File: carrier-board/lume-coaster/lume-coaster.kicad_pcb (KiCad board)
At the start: 2 copper layers, 85 x 40 mm, 37 parts, among them J1_BOT T5AI_CORE_BOT, J1_TOP T5AI_CORE_TOP, J2 ILI9341_SPI_LCD, J3 ACTIVE_CHIME, J4_HARNESS TO_MODULE_CN1, J5 USB-C, Q1 AO3401, SW1 MODE, SW2 UP, SW3 DOWN

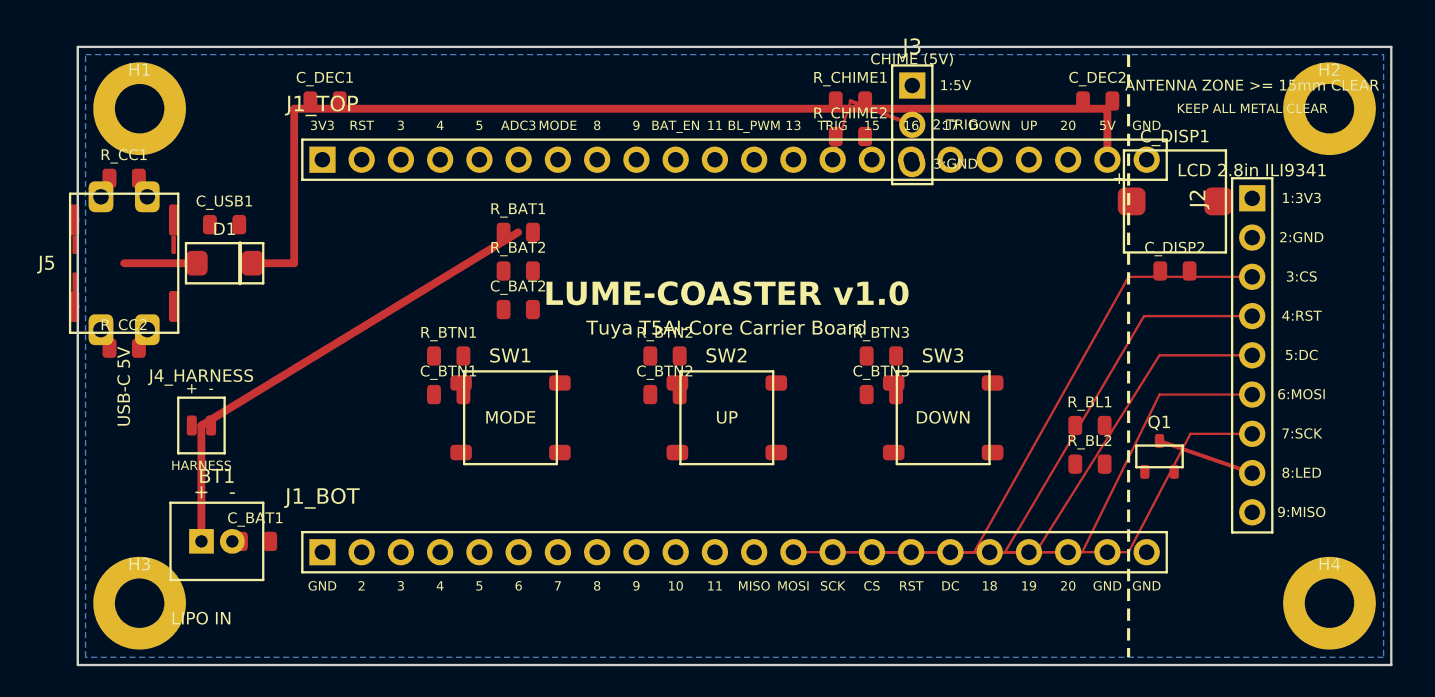
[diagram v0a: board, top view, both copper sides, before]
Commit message: feat(week1): lume-coaster carrier board - fab-ready
- Tuya T5AI-Core (T5-E1) carrier, 85x40mm 2-layer
- 2x1x22 PinSocket headers, 25.4mm center-to-center
- Full GND pour on B.Cu with on-disk filled polygon
- ERC 0/0/0, DRC 0 violations / 0 unconnected / 0 footprint errors
- Gerbers + drill archive verified (G36/G37 solid copper fill present)
- Untrack .history submodule, KiCad lockfiles, scratch generators
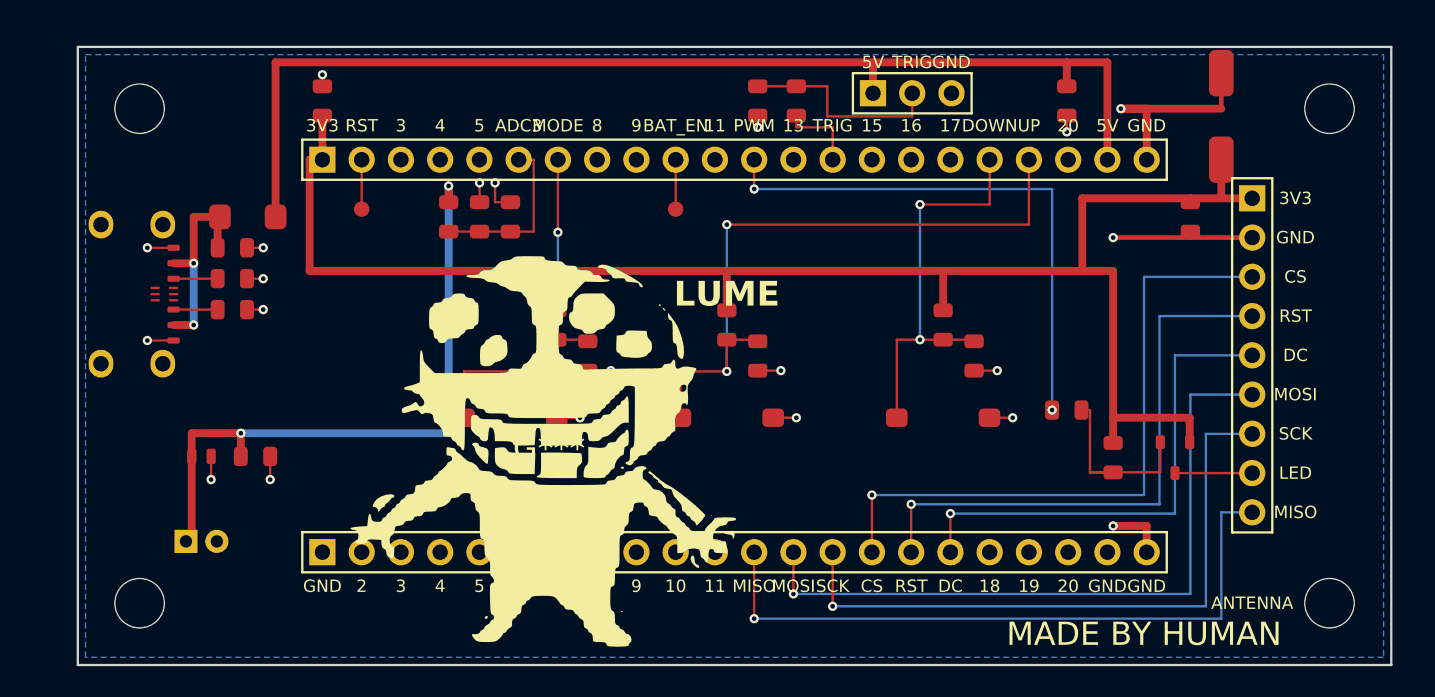
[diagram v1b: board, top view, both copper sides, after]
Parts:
- removed the J4_HARNESS at (8.00, 24.5)
- added G***: LOGO, LOGO, F.Cu at (30.5, 26.0)
- added J4_HARNESS: TO_MODULE_CN1, Connector_JST:JST_GH_SM02B-GHS-TB_1x02-1MP_P1.25mm_Horizontal, F.Cu at (8.00, 26.5)
- added TP1: BATT_EN, TestPoint:TestPoint_Pad_D1.0mm, F.Cu at (38.7, 10.5)
- added TP2: TS_RST, TestPoint:TestPoint_Pad_D1.0mm, F.Cu at (18.4, 10.5)
- C_BAT1, C_BAT2, C_BTN1, C_BTN2, C_BTN3, C_DEC1, C_DEC2, C_DISP2, C_USB1: footprint Resistor_SMD:R_0805_2012Metric -> Capacitor_SMD:C_0805_2012Metric
- H1, H2, H3, H4: value (none) -> MountingHole; footprint MountingHole:MountingHole_3.2mm_M3_Pad -> MountingHole:MountingHole_3.2mm_M3
- J3: footprint Connector_PinHeader_2.54mm:PinHeader_1x03_P2.54mm_Vertical -> Connector_PinHeader_2.54mm:PinHeader_1x03_P2.54mm_Horizontal
- Q1: value AO3401 -> AO3401A
- SW1, SW2, SW3: footprint Button_Switch_SMD:SW_Push_1P1T_NO_6x6mm_H9.5mm -> Button_Switch_SMD:SW_Push_1TS009xxxx-xxxx-xxxx_6x6x5mm
- moved J5 14.3 mm to (0.00, 0.00), turned to 0 degrees
- moved R_CC1 9.55 mm to (10.0, 15.0)
- moved C_BTN1 9.34 mm to (33.0, 20.0)
- moved R_CC2 7.43 mm to (10.0, 17.0)
- moved R_BTN1 7.28 mm to (31.0, 18.0)
- moved C_BTN2 6.50 mm to (44.0, 20.0)
- moved C_BTN3 6.50 mm to (58.0, 20.0)
- moved R_CHIME2 6.43 mm to (44.0, 3.50)
- moved C_DISP1 6.26 mm to (74.0, 4.50)
- moved C_BAT2 6.02 mm to (28.0, 11.0)
- moved C_BAT1 5.50 mm to (11.5, 26.5)
- moved R_BAT1 4.61 mm to (24.0, 11.0)
- moved R_BTN2 4.47 mm to (42.0, 18.0)
- moved R_BTN3 4.47 mm to (56.0, 18.0)
- moved R_BAT2 4.30 mm to (26.0, 11.0)
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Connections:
- net CC1 renamed /CC1
- net CC2 renamed /CC2
- net LCD_DC renamed /LCD_DC
- net LCD_LED renamed /LCD_LED
- net LCD_RST renamed /LCD_RST
- net SPI0_CS renamed /SPI0_CS
- net SPI0_MISO renamed /SPI0_MISO
- net SPI0_MOSI renamed /SPI0_MOSI
- net SPI0_SCK renamed /SPI0_SCK
- net VBAT renamed /VBAT
- BT1 pad 2: GND -> /GND
- C_BAT1 pad 2: GND -> /GND
- C_BAT2 pad 1: BATT_SENSE -> /GND
- C_BAT2 pad 2: GND -> /BATT_SENSE
- C_BTN1 pad 1: BTN_MODE -> /BTN_MODE
- C_BTN1 pad 2: GND -> /GND
- C_BTN2 pad 1: BTN_UP -> /BTN_UP
- C_BTN2 pad 2: GND -> /GND
- C_BTN3 pad 1: BTN_DOWN -> /BTN_DOWN
- C_BTN3 pad 2: GND -> /GND
- C_DEC1 pad 1: +3V3 -> /GND
- C_DEC1 pad 2: GND -> /+3V3
- C_DEC2 pad 1: +5V -> /+5V
- C_DEC2 pad 2: GND -> /GND
- C_DISP1 pad 1: +3V3 -> /+3V3
- C_DISP1 pad 2: GND -> /GND
- C_DISP2 pad 1: +3V3 -> /+3V3
- C_DISP2 pad 2: GND -> /GND
- C_USB1 pad 1: VBUS -> /VBUS
- C_USB1 pad 2: GND -> /GND
- D1 pad 1: VBUS -> /+5V
- D1 pad 2: +5V -> /VBUS
- J1_BOT pad 1: GND -> /GND
- J1_BOT pad 21: GND -> /GND
- J1_BOT pad 22: GND -> /GND
- J1_TOP pad 1: +3V3 -> /+3V3
- J1_TOP pad 10: BATT_EN -> /BATT_EN
- J1_TOP pad 12: LCD_BL_GATE -> /LCD_BL_PWM
- J1_TOP pad 14: CHIME_TRIG -> /CHIME_TRIG
- J1_TOP pad 18: BTN_DOWN -> /BTN_DOWN
- J1_TOP pad 19: BTN_UP -> /BTN_UP
- J1_TOP pad 2: TS_RST -> /TS_RST
- J1_TOP pad 21: +5V -> /+5V
- J1_TOP pad 22: GND -> /GND
- J1_TOP pad 6: BATT_SENSE -> /BATT_SENSE
- J1_TOP pad 7: BTN_MODE -> /BTN_MODE
- J2 pad 1: +3V3 -> /+3V3
- J2 pad 2: GND -> /GND
- J3 pad 1: +5V -> /+5V
- J3 pad 2: CHIME_OUT -> /CHIME_OUT
- J3 pad 3: GND -> /GND
- J5 pad A1: GND -> /GND
- J5 pad A12: GND -> /GND
- J5 pad A4: VBUS -> /VBUS
- J5 pad A8: GND -> (no net)
- J5 pad A9: VBUS -> /VBUS
- J5 pad B1: GND -> /GND
- J5 pad B12: GND -> /GND
- J5 pad B4: VBUS -> /VBUS
- J5 pad B9: VBUS -> /VBUS
- Q1 pad 1: LCD_BL_GATE -> /LCD_BL_GATE
- Q1 pad 2: +3V3 -> /+3V3
- R_BAT1 pad 2: BATT_SENSE -> /BATT_SENSE
- R_BAT2 pad 1: BATT_SENSE -> /GND
- R_BAT2 pad 2: GND -> /BATT_SENSE
- R_BL1 pad 1: LCD_BL_GATE -> /+3V3
- R_BL1 pad 2: +3V3 -> /LCD_BL_GATE
- R_BL2 pad 1: LCD_BL_GATE -> /LCD_BL_PWM
- R_BL2 pad 2: LCD_BL_GATE -> /LCD_BL_GATE
- R_BTN1 pad 1: BTN_MODE -> /+3V3
- R_BTN1 pad 2: +3V3 -> /BTN_MODE
- R_BTN2 pad 1: BTN_UP -> /+3V3
- R_BTN2 pad 2: +3V3 -> /BTN_UP
- R_BTN3 pad 1: BTN_DOWN -> /+3V3
- R_BTN3 pad 2: +3V3 -> /BTN_DOWN
- R_CC1 pad 2: GND -> /GND
- R_CC2 pad 2: GND -> /GND
- R_CHIME1 pad 1: CHIME_TRIG -> /CHIME_OUT
- R_CHIME1 pad 2: CHIME_OUT -> /CHIME_TRIG
- R_CHIME2 pad 1: CHIME_OUT -> /CHIME_OUT
- R_CHIME2 pad 2: GND -> /GND
- SW1 pad 1: BTN_MODE -> /BTN_MODE
- SW1 pad 2: BTN_MODE -> /GND
- SW2 pad 1: BTN_UP -> /BTN_UP
- SW2 pad 2: BTN_UP -> /GND
- SW3 pad 1: BTN_DOWN -> /BTN_DOWN
- SW3 pad 2: BTN_DOWN -> /GND
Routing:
- net /+3V3: track 0.00 -> 106.6 mm
- net /+5V: track 0.00 -> 73.7 mm
- net +5V: track 68.6 -> 0.00 mm
- net /GND: track 0.00 -> 51.6 mm, vias 0 -> 21
- net /SPI0_MISO: track 0.00 -> 43.4 mm, vias 0 -> 1
- net /BTN_UP: track 0.00 -> 43.4 mm, vias 0 -> 2
- net /LCD_BL_PWM: track 0.00 -> 35.5 mm, vias 0 -> 2
- net /BTN_MODE: track 0.00 -> 26.9 mm, vias 0 -> 2
- net /BTN_DOWN: track 0.00 -> 26.3 mm, vias 0 -> 2
- net /CHIME_OUT: track 0.00 -> 13.4 mm
- net /VBUS: track 0.00 -> 13.3 mm, vias 0 -> 2
- net /LCD_BL_GATE: track 0.00 -> 12.6 mm
- net /BATT_SENSE: track 0.00 -> 11.1 mm
- net /VBAT: track 31.5 -> 42.5 mm, vias 0 -> 2
- net /SPI0_SCK: track 31.8 -> 41.8 mm, vias 0 -> 1
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- added copper zone on B.Cu, net /GND
- removed copper zone on B.Cu, net GND
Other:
- rule pad_to_mask_clearance: 0.05 -> 0
- board text added: "ANTENNA"
- board text added: "LUME"
- board text added: "MADE BY HUMAN"
- board text removed: "ANTENNA ZONE >= 15mm CLEAR"
- board text removed: "CHIME (5V)"
- board text removed: "KEEP ALL METAL CLEAR"
- board text removed: "LCD 2.8in ILI9341"
- board text removed: "LIPO IN"
- board text removed: "LUME-COASTER v1.0"
- board text removed: "Tuya T5AI-Core Carrier Board"
- board text removed: "USB-C 5V"
